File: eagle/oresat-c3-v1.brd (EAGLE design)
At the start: 99.8 x 94.7 mm, 112 parts, among them J1 J-SAMTEC-TFM-110-X1-XXX-D-RA, J10 2X8X1.27, J11 2X8X1.27, J12 2X8X1.27, J2 U.FL, J3 U.FL, J4 U.FL, J6 J-SAMTEC-TFM-120-X1-XXX-D-RA, J7 FTSH-105-XX-X-DV-K, J9 2X8X1.27, U1 MAX892LEUA+T21-0036K-L, U2 TCAN330, U3 TCAN330, U4 TPS259621 - eFuse, U5 TPS62111RSA, U6 MAX6374KA-T21-0078H-L, U7 STM32F446RE, X1 16MHZ-2.5x2mm

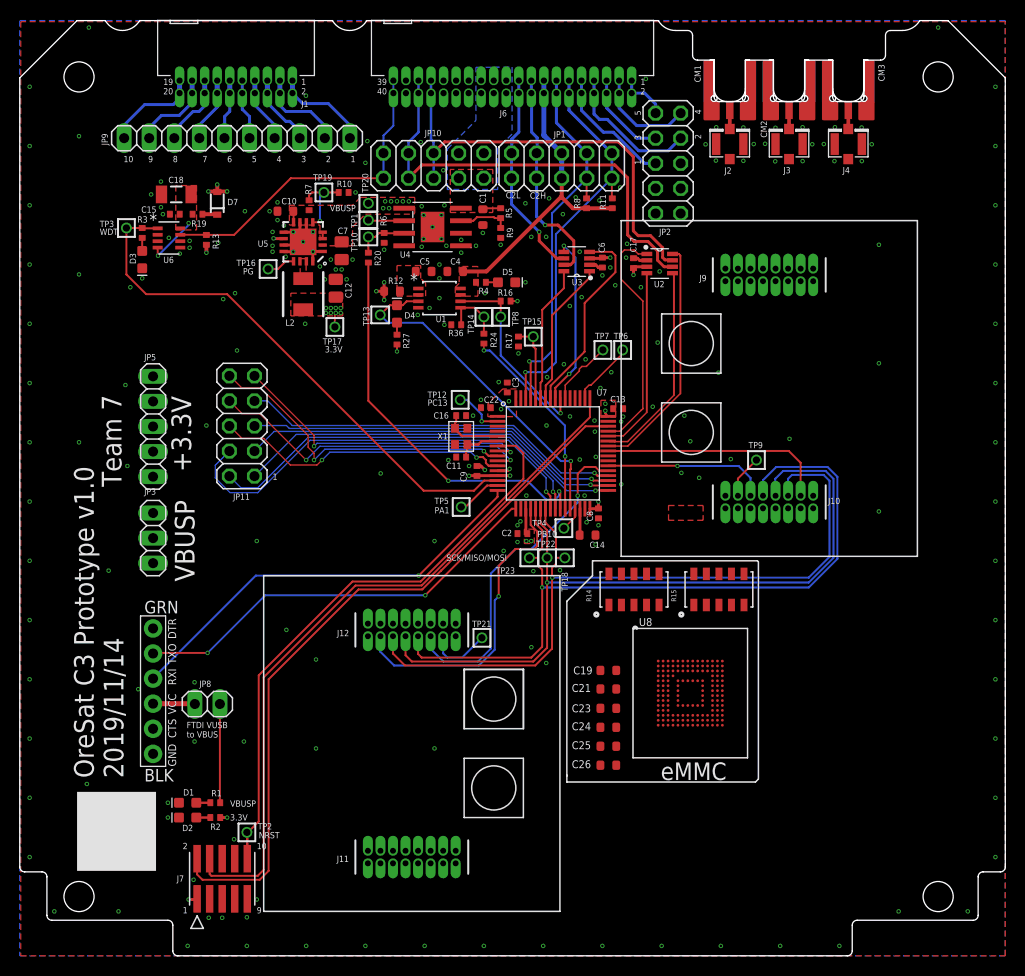
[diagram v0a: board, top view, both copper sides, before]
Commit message: Added eMMC
Almost completed adding eMMC
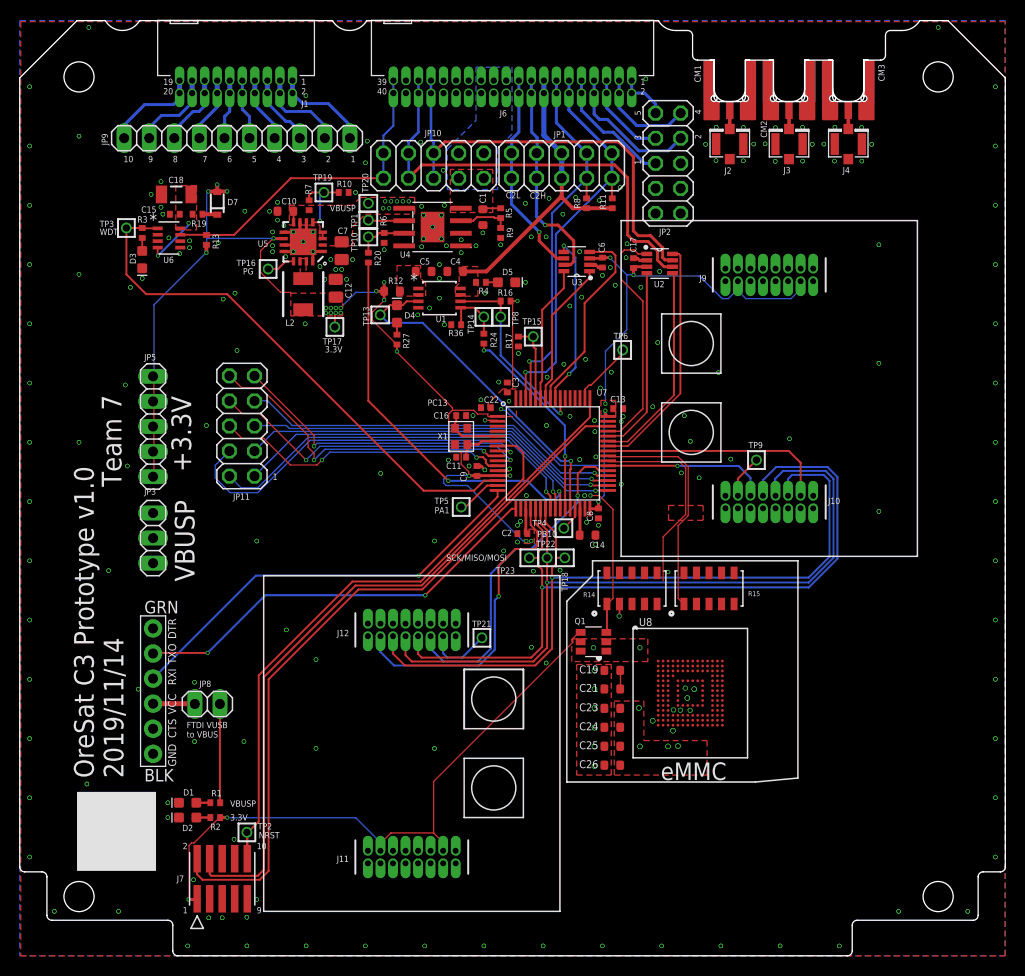
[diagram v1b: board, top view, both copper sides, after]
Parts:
- removed TP12, TP7: TEST-POINT, Tova:2MM-TEST-POINT
- added Q1: MOSFET-PCH-SOT23-6, Q-MOSFET-PCH-SOT23-6:SOT23-6
- C21: value 1u -> 0.1u
- R14, R15: value (none) -> 10k
- U8: value (none) -> SFEM016GB1EM1TO-A-HG-111-STD
- moved R15 1.00 mm to (69.8, 37.2)
- moved C19 0.40 mm to (60.0, 28.9)
- moved C21 0.40 mm to (60.0, 27.0), turned to 180 degrees
- moved C23 0.40 mm to (60.0, 25.1), turned to 180 degrees
- moved C24 0.40 mm to (60.0, 23.1), turned to 180 degrees
- moved C25 0.40 mm to (60.0, 21.2), turned to 180 degrees
- moved C26 0.40 mm to (60.0, 19.3), turned to 180 degrees
- moved R14 0.22 mm to (62.0, 37.2)
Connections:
- removed net N$6: C19.1, U8.C2
- removed net PC13: TP12.1, U7.2
- removed net PD2: TP7.1, U7.54
- new net MMC_PWR: Q1.3, R14.1, U7.2
- new net MMC_VDD: C23.1, C24.1, C25.1, C26.1, Q1.1, Q1.2, Q1.5, Q1.6, U8.C6, U8.E6, U8.F5, U8.J10, U8.K9, U8.M4, U8.N4, U8.P3, U8.P5
- new net SDIO_CK: R14.8, U7.53, U8.M6
- new net SDIO_CMD: R14.9, U7.54, U8.M5
- new net SDIO_D0: R14.4, U7.39, U8.A3
- new net SDIO_D1: R15.1, U7.40, U8.A4
- new net SDIO_D2: R15.2, U7.51, U8.A5
- new net SDIO_D3: R14.3, U7.52, U8.A1, U8.B2
- new net SDIO_D4: R15.8, U8.A2, U8.B3
- new net SDIO_D5: R15.7, U8.B4, U8.C5
- new net SDIO_D6: R15.4, U8.A6, U8.B5
- new net SDIO_D7: R15.6, U8.A7, U8.B6
- new net SDIO_RST: R14.2, U8.K5
- new net VDDI: C19.1, C21.1, U8.C1, U8.C2
- net 3.3V: now also Q1.4; no longer C21.1, C23.1, C24.1, C25.1, C26.1, U8.C6, U8.E6, U8.F5, U8.J10, U8.K9, U8.M4, U8.N4, U8.P3, U8.P5
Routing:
- net 3.3V: track 24.9 -> 249.5 mm, vias 31 -> 32
- net MMC_PWR: track 0.00 -> 30.8 mm, vias 0 -> 2
- net SDIO_D1: track 0.00 -> 23.2 mm
- net SDIO_D0: track 0.00 -> 21.2 mm
- net PD2: track 6.72 -> 0.00 mm
- net PC13: track 5.10 -> 0.00 mm, vias 1 -> 0
- net VDDI: track 0.00 -> 1.90 mm
- net SDIO_RST: track 0.00 -> 1.24 mm, vias 0 -> 2
- net MMC_VDD: track 0.00 -> 0.22 mm, vias 0 -> 11
- net SDIO_CK: track 0.00 -> 0.04 mm, vias 0 -> 1
- net SDIO_CMD: track 0.00 -> 0.04 mm, vias 0 -> 1
- net GND: vias 222 -> 464
- added copper zone on layer 15, net MMC_VDD

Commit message: integrated 2 AX5043 radios and connected up the eMMC
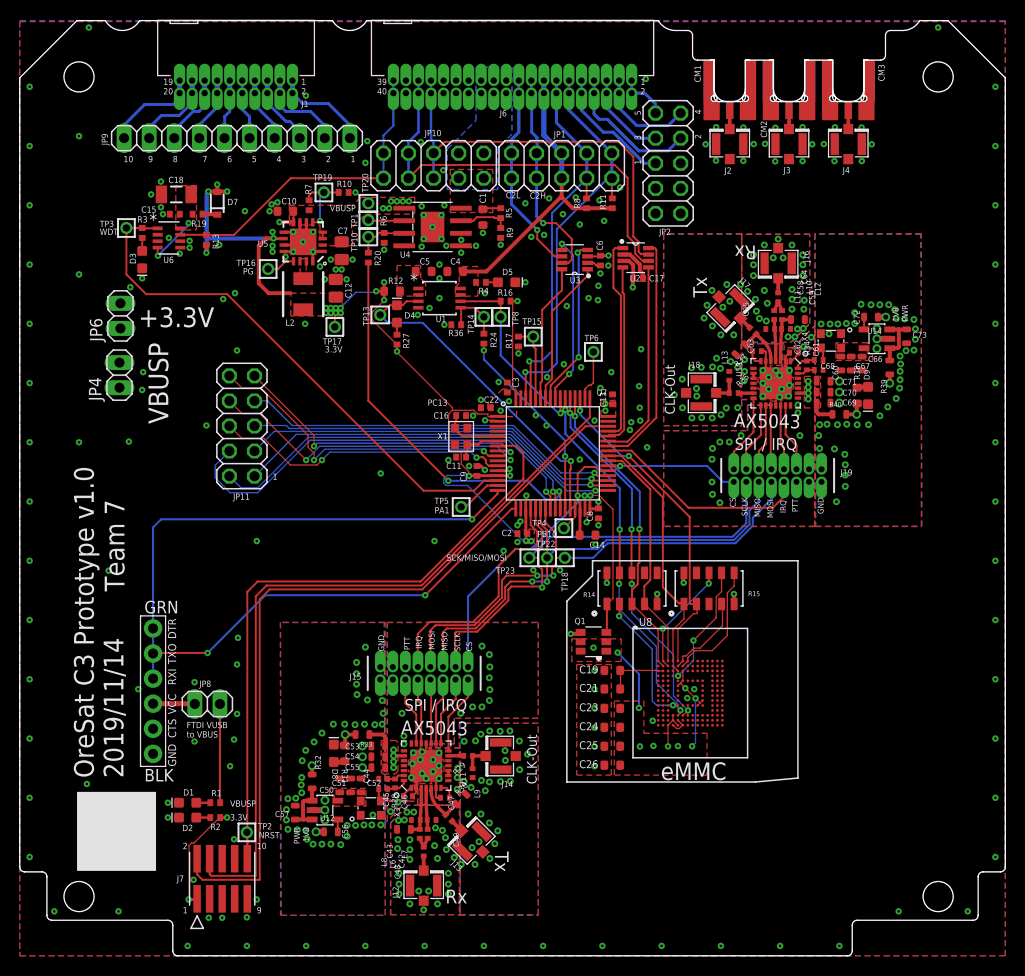
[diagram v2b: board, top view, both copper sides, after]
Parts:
- removed J10, J11, J9: 2X8X1.27, 2x8x1.27:2X8X1.27
- removed JP3: (no value), pinhead:1X03
- removed JP5: (no value), pinhead:1X05
- removed TP21, TP9: TEST-POINT, Tova:2MM-TEST-POINT
- added C42, C43, C58, C59: 8.2p, oresat-rcl:.0402-C-NOSILK
- added C44, C45, C60, C61: 1n, oresat-rcl:.0402-C-NOSILK
- added C46, C47, C62, C63: 82p, oresat-rcl:.0402-C-NOSILK
- added C48, C49, C64, C65: 22p, oresat-rcl:.0402-C-NOSILK
- added C50, C53, C66, C69: 22n, oresat-rcl:.0603-C-NOSILK
- added C51, C54, C67, C70: NP, oresat-rcl:.0603-C-NOSILK
- added C52, C55, C68, C71: 4.7u, oresat-rcl:.0603-C-NOSILK
- added C56, C72: 10n, oresat-rcl:.0603-C-NOSILK
- added C57, C73: 1u, oresat-rcl:.0603-C-NOSILK
- added D8, D9: GREEN, SparkFun-LED:LED-0603
- added J13, J14, J16, J17, J18: U.FL, SparkFun-Connectors:U.FL
- added J15, J19: HARWIN-2X8X1.27, J-Harwin-M50-3610842R-2X8X1.27_Male :2X8X1.27
- added JP4, JP6: (no value), J-2X8X1.27:1X02
- added L10, L11, L6, L7: 43n, oresat-rcl:.0402-C-NOSILK
- added L12, L13, L8, L9: 91n, oresat-rcl:.0603-C-NOSILK
- added R28, R34: 150, oresat-rcl:.0402-C-NOSILK
- added R29, R35: 0, oresat-rcl:.0402-C-NOSILK
- added R30, R37: NP, oresat-rcl:.0402-C-NOSILK
- added R31, R38: 1.5k, oresat-rcl:.0603-B-NOSILK
- added R32, R33, R39, R40: 0, oresat-rcl:.0603-C-NOSILK
- added U11, U13: U-ONSEMI-AX5043, U-ON-Semi-AX5043-radio:QFN28-5X5-WITH-CENTER-PAD
- added U12, U14: LP2985XX-N, U-TI-LP2985XX-N-linear-reg:SOT-23
- added X3, X4: TAITIEN-TY, X-Taitien-TY-TCXO:2.5X2.0
- D3: value RED -> GREEN
- D4: value AMBER -> GREEN
- J12: value 2X8X1.27 -> U.FL; device 2x8x1.27:2X8X1.27 -> SparkFun-Connectors:U.FL
- moved J12 25.9 mm to (40.9, 7.11), turned to 90 degrees
- moved TP6 2.97 mm to (58.1, 61.1)
- moved U2 2.50 mm to (62.4, 70.7)
- moved C17 1.63 mm to (62.6, 68.6), turned to 180 degrees
- moved C13 1.11 mm to (60.0, 56.4), turned to 270 degrees
- moved C6 0.28 mm to (58.8, 70.4)
- moved U3 0.28 mm to (56.2, 70.5)
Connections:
- removed net RADIO1_SYSCLK: J12.3, TP21.1
- removed net RADIO2_SYSCLK: J10.3, TP9.1
- new net 1V1: C50.1, C51.1, C52.1, U12.5, X3.4
- new net 1V2: C66.1, C67.1, C68.1, U14.5, X4.4
- new net ANTN1: C42.2, L7.2, U11.4
- new net ANTN2: C58.2, L11.2, U13.4
- new net ANTP2: C43.2, L6.2, L8.1, U11.3
- new net ANTP3: C49.2, L9.2, U11.5
- new net ANTP4: C59.2, L10.2, L12.1, U13.3
- new net ANTP5: C65.2, L13.2, U13.5
- new net CLKN1: C44.1, R28.1, U11.27
- new net CLKN2: C60.1, R34.1, U13.27
- new net CLKP1: C45.1, R28.2, U11.28
- new net CLKP2: C61.1, R34.2, U13.28
- new net CS1: J15.1, U11.14
- new net CS2: J19.1, U13.14
- new net GNDR: C43.1, C44.2, C46.2, C47.1, C50.2, C51.2, C52.2, C53.2, C54.2, C55.2, C56.2, C57.2, C59.1, C60.2, C62.2, C63.1, C66.2, C67.2, C68.2, C69.2, C70.2, C71.2, C72.2, C73.2, D8.C, D9.C, J15.15, J19.15, L11.1, L12.2, L13.1, L7.1, L8.2, L9.1, R30.2, R37.2, U11.2, U11.6, U11.PAD, U12.2, U13.2, U13.6, U13.PAD, U14.2, X3.2, X4.2
- new net IRQ1: J15.9, U11.19
- new net IRQ2: J19.9, U13.19
- new net LEDPWR1: D8.A, R31.2
- new net LEDPWR2: D9.A, R38.2
- new net MISO1: J15.5, U11.16
- new net MISO2: J19.5, U13.16
- new net MOSI1: J15.7, U11.17
- new net MOSI2: J19.7, U13.17
- new net N$10: C56.1, U12.4
- new net N$11: C42.1, C48.2, L6.1
- new net N$12: C45.2, X3.3
- new net N$13: U13.10, U13.9
- new net N$14: C62.1, U13.1
- new net N$15: C63.2, U13.7
- new net N$16: C72.1, U14.4
- new net N$17: C58.1, C64.2, L10.1
- new net N$18: C61.2, X4.3
- new net N$7: U11.10, U11.9
- new net N$8: C46.1, U11.1
- new net N$9: C47.2, U11.7
- new net PWRAMP1: J15.11, U11.20
- new net PWRAMP2: J19.11, U13.20
- new net RADIO1_PTT: J15.12
- new net RADIO2_PTT: J19.12
- new net REF-OUT1: J14.FEED, R29.2, R30.1
- new net REF-OUT2: J18.FEED, R35.2, R37.1
- new net RX1: C48.1, J12.FEED
- new net RX2: C64.1, J16.FEED
- new net SCLK1: J15.3, U11.15
- new net SCLK2: J19.3, U13.15
- new net SYSCLK1: R29.1, U11.13
- new net SYSCLK2: R35.1, U13.13
- new net TX1: C49.1, J13.FEED
- new net TX2: C65.1, J17.FEED
- net 3.3V: now also C53.1, C54.1, C55.1, C57.1, C69.1, C70.1, C71.1, C73.1, JP6.1, JP6.2, R31.1, R32.1, R32.2, R33.1, R33.2, R38.1, R39.1, R39.2, R40.1, R40.2, U11.23, U12.1, U12.3, U13.23, U14.1, U14.3; no longer J11.13, J11.3, J9.13, J9.3, JP5.1, JP5.2, JP5.3, JP5.4, JP5.5
- net GND: no longer J10.1, J10.10, J10.12, J10.14, J10.15, J10.16, J10.2, J10.4, J10.6, J10.8, J11.1, J11.10, J11.12, J11.14, J11.15, J11.16, J11.2, J11.4, J11.6, J11.8, J12.1, J12.10, J12.12, J12.14, J12.15, J12.16, J12.2, J12.4, J12.6, J12.8, J9.1, J9.10, J9.12, J9.14, J9.15, J9.16, J9.2, J9.4, J9.6, J9.8
- net RADIO1_CS: now also J15.2; no longer J12.5
- net RADIO1_IRQ: now also J15.10; no longer J12.13
- net RADIO2_CS: now also J19.2; no longer J10.5
- net RADIO2_IRQ: now also J19.10; no longer J10.13
- net SPI1_MISO: now also J15.6, J19.6; no longer J10.9, J12.9
- net SPI1_MOSI: now also J15.8, J19.8; no longer J10.11, J12.11
- net SPI1_SCK: now also J15.4, J19.4; no longer J10.7, J12.7
- net VBUSP: now also JP4.1, JP4.2; no longer JP3.1, JP3.2, JP3.3
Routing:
- net 3.3V: track 249.5 -> 376.2 mm, vias 32 -> 48
- net SDIO_CK: track 0.04 -> 37.5 mm, vias 1 -> 4
- net SDIO_CMD: track 0.04 -> 37.2 mm, vias 1 -> 4
- net SDIO_D2: track 0.13 -> 33.3 mm, vias 0 -> 2
- net SDIO_D3: track 0.17 -> 31.7 mm, vias 0 -> 2
- net SPI1_SCK: track 79.9 -> 51.9 mm
- net SPI1_MISO: track 77.8 -> 51.2 mm, vias 1 -> 2
- net VBUSP: track 100.0 -> 74.5 mm
- net SPI1_MOSI: track 77.8 -> 53.6 mm, vias 1 -> 2
- net MMC_VDD: track 0.22 -> 20.8 mm, vias 11 -> 9
- net GNDR: track 0.00 -> 13.5 mm, vias 0 -> 262
- net SDIO_D5: track 0.00 -> 13.5 mm, vias 0 -> 2
- net SDIO_RST: track 1.24 -> 14.0 mm
- net SDIO_D7: track 0.00 -> 12.6 mm
- net SDIO_D4: track 0.00 -> 11.6 mm, vias 0 -> 2
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- added copper zone on layer 1, net 1V1
- added copper zone on layer 1, net 1V2
- added copper zone on layer 1, net GNDR
- added copper zone on layer 15, net GNDR
- added copper zone on layer 16, net GNDR
- added copper zone on layer 2, net GNDR
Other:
- board text added: "1V8"
- board text added: "AX5043"
- board text added: "CLK-Out"
- board text added: "CS"
- board text added: "GND"
- board text added: "IRQ"
- board text added: "MISO"
- board text added: "MOSI"
- board text added: "PTT"
- board text added: "PWR"
- board text added: "Rx"
- board text added: "SCLK"
- board text added: "SPI / IRQ"
- board text added: "Tx"

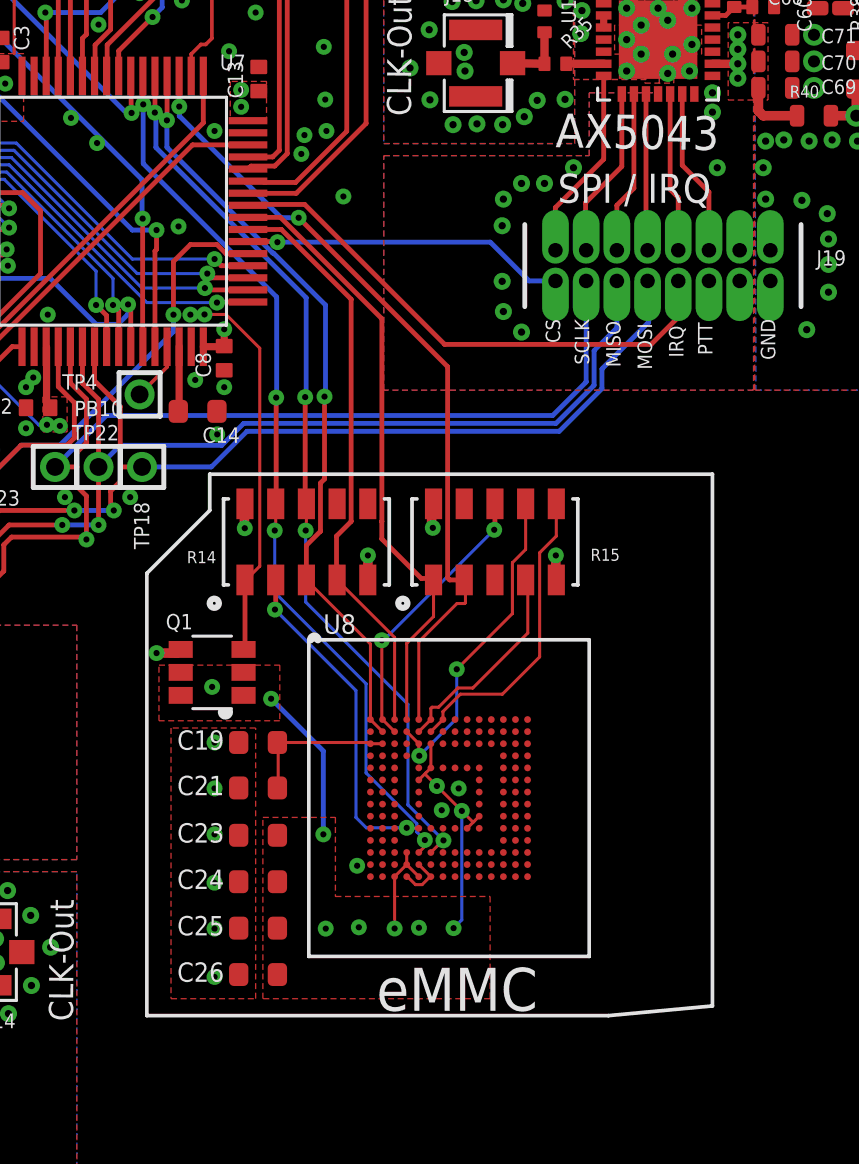
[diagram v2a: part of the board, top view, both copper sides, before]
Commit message: Make changes to oresat-c3-v1 board
Fix eMMC pin out to better match datasheet
Route data lines to match lengths
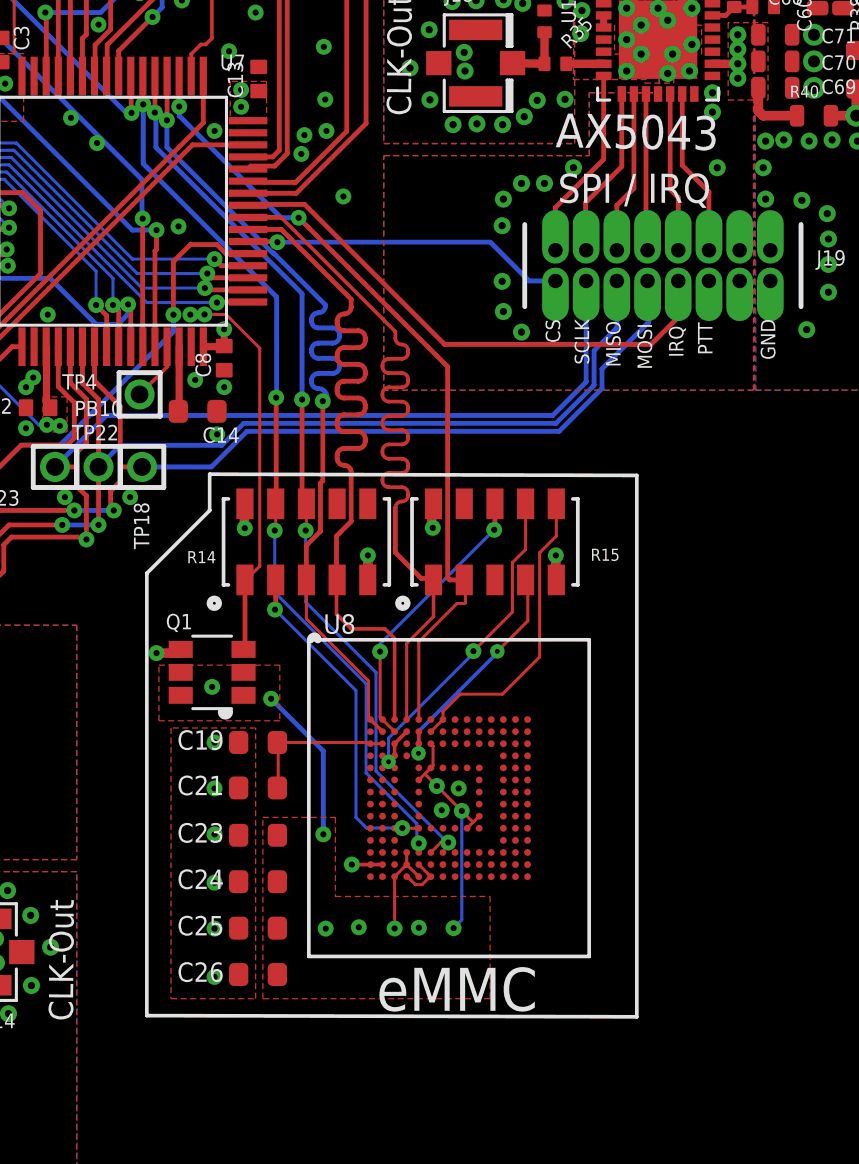
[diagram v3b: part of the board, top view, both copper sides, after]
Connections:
- net GND: now also U8.A6, U8.J5, U8.N1
- net MMC_VDD: now also U8.P7
- net SDIO_D5: now also U8.C3, U8.D3; no longer U8.C5
- net SDIO_D6: now also U8.C5; no longer U8.A6
- net VDDI: no longer U8.C1
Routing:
- net SDIO_D1: track 25.6 -> 33.4 mm
- net SDIO_D0: track 24.9 -> 32.7 mm
- net SDIO_D3: track 31.7 -> 35.5 mm
- net SDIO_D6: track 8.70 -> 10.00 mm, vias 0 -> 2
- net GND: track 24.1 -> 25.3 mm
- net SDIO_D5: track 13.5 -> 14.6 mm
